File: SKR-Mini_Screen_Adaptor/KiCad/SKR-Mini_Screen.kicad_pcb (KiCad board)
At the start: 2 copper layers, 22.9 x 43.2 mm, 6 parts, among them J1 Board_EXP1, J2 Board_SPI, J3 Screen_EXP1, J4 Screen_EXP2

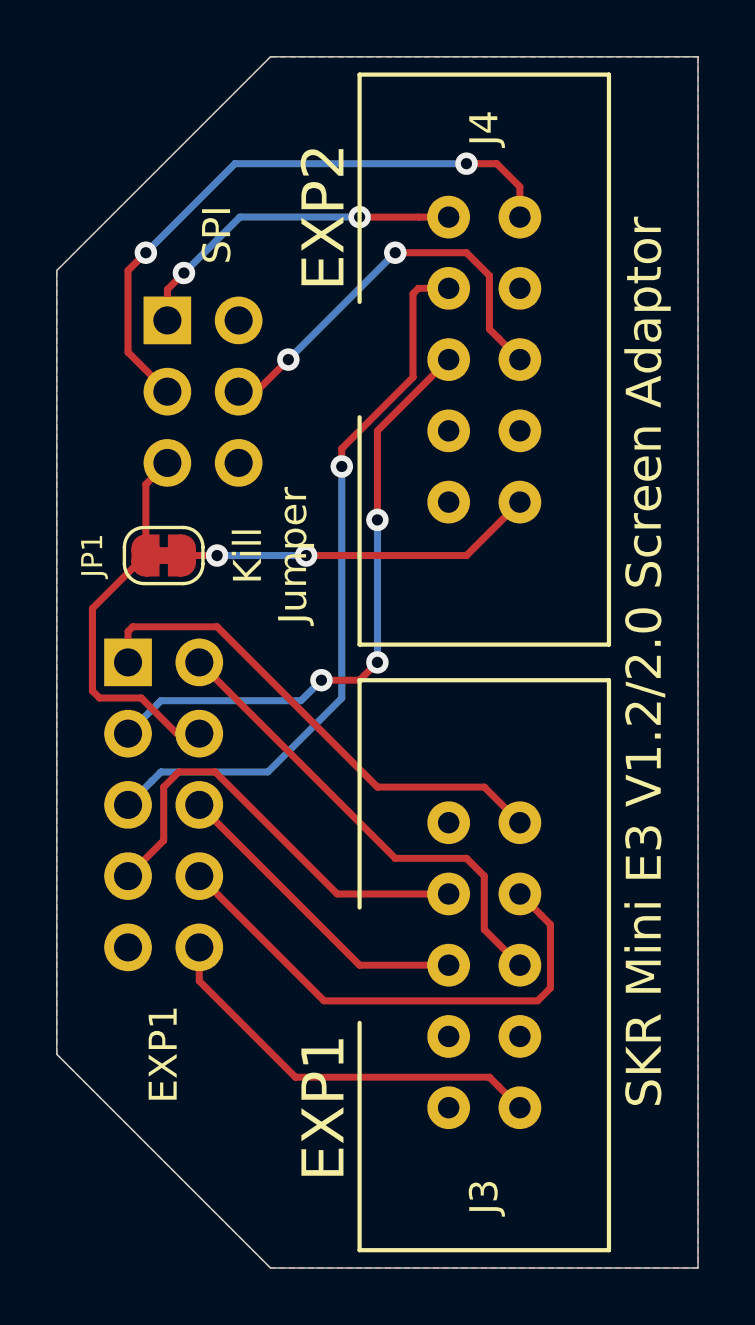
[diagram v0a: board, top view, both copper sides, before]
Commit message: Improve compatibility with BTT Display
Board and Schematic changed to accept a reset signal from either the "Reset" line or the "Kill" line and changes the default configuration to use the "Reset" line.  Big Tree Tech boards are configured by default to use the reset line and Fysetc boards are configured by default to use both the reset and kill lines.  The proposed changes should allow the reset button on either the Fysetc or the BTT display to work without requiring the user to reconfigure the adapter or display.  It also gives the option to reconfigure the adapter to use the "Kill" line or to disable the function if desired.
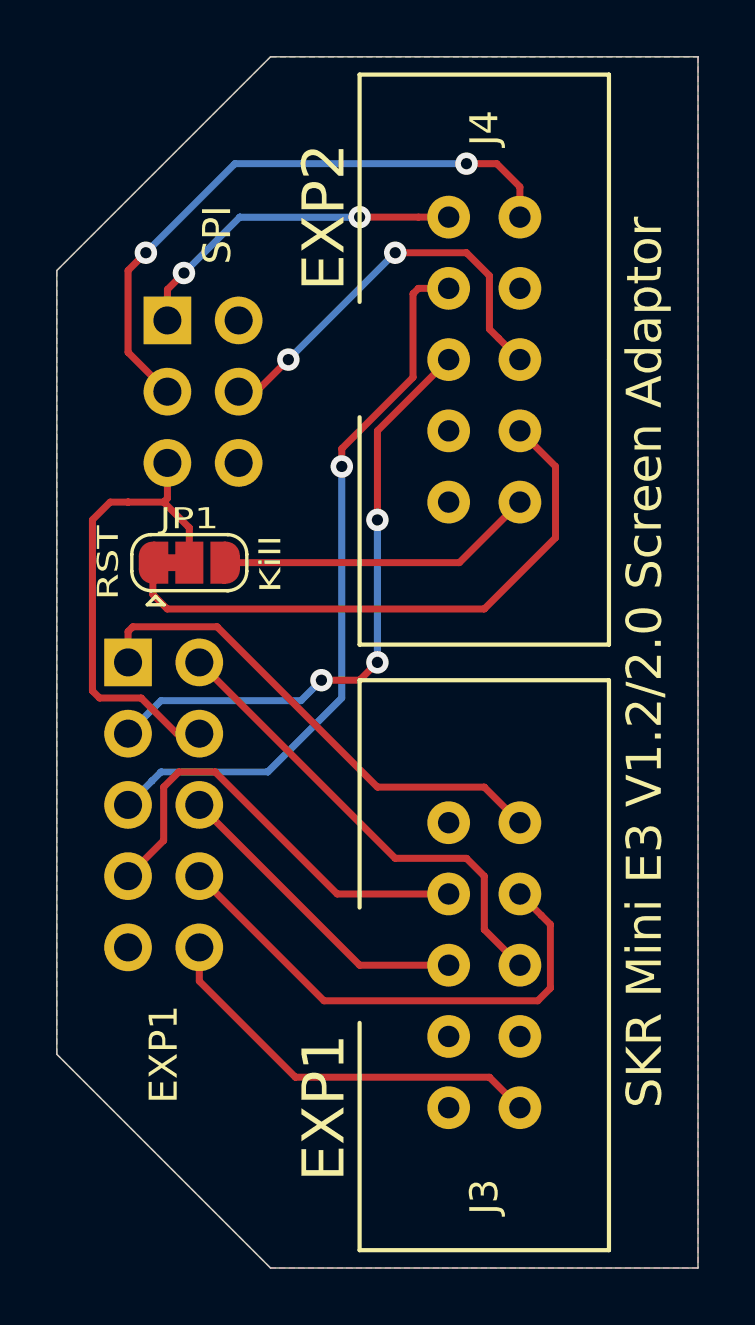
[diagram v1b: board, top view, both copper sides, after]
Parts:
- JP1: value Jumper_NC_Small -> SolderJumper_3_Bridged12; footprint Jumper:SolderJumper-2_P1.3mm_Bridged_RoundedPad1.0x1.5mm -> Jumper:SolderJumper-3_P1.3mm_Bridged12_RoundedPad1.0x1.5mm
- moved JP1 0.95 mm to (127.9, 103.1)
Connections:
- J3 pad 1: (no net) -> /Beep
- J3 pad 7: (no net) -> unconnected-(J3-Pad7)
- J3 pad 8: (no net) -> unconnected-(J3-Pad8)
- J4 pad 4: (no net) -> unconnected-(J4-Pad4)
- J4 pad 7: (no net) -> unconnected-(J4-Pad7)
- J4 pad 8: (no net) -> /Reset
- JP1 pad 1: /RST -> /Reset
- JP1 pad 2: /Kill -> /RST
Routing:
- net /Reset: track 0.00 -> 21.1 mm
- net /RST: track 13.0 -> 17.3 mm
- net /Kill: track 12.8 -> 11.4 mm, vias 2 -> 0
- added copper zone on F.Cu, net /GND
- removed copper zone on F.Cu, net /+5V
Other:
- net class Default removed
- board text added: "Kill"
- board text added: "RST"
- board text added: "T. Abraham RevB"
- board text removed: "Kill Jumper"
- board text removed: "T. Abraham RevA"
